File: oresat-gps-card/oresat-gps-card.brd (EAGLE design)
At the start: 99.8 x 94.6 mm, 373 parts, among them J1 ORESAT-DEBUG-CONNECTOR-CARD, J100 DM3BT-DSF-PEJS, J102 FTSH-105-XX-X-DV-K, J4 TFM-120-01-L-D-RA, Q1 MMBT2907, Q2 PMV45EN, Q3 DMP2240UDM, Q4 PMV45EN, Q5 MOSFET-PCH-SOT23-6, Q6 MOSFET-PCH-SOT23-6, U1 RCLAMP0504FB, U10 TLVH431, U11 TCAN330, U12 MIC842LYC5, U13 MIC842LYC5, U14 MAX4211FETE, U15 TPS62112, U16 MAX7310ATE, U17 25AAXX, U18 RCLAMP0504FB, U19 BP2G+, U2 TPS2051CDBVR, U20 MAX8510EXK29+T, U21 SF14-1575F5UUA1, U22 LT1719S6, U23 MAX2771ETI+, U24 VENUS838LPX-L, U3 THGBMJG7C2LBAU8, U4 SN74LVC1G07DCK, U5 SKY65723-81, U6 7Q-16.368MBG-T, U7 OSD3358-512M-BSM, U8 MAX8510EXK29+T, U9 MAX8510EXK29+T, Y1 24MHz, Y2 ABS07-32.768KHZ-T

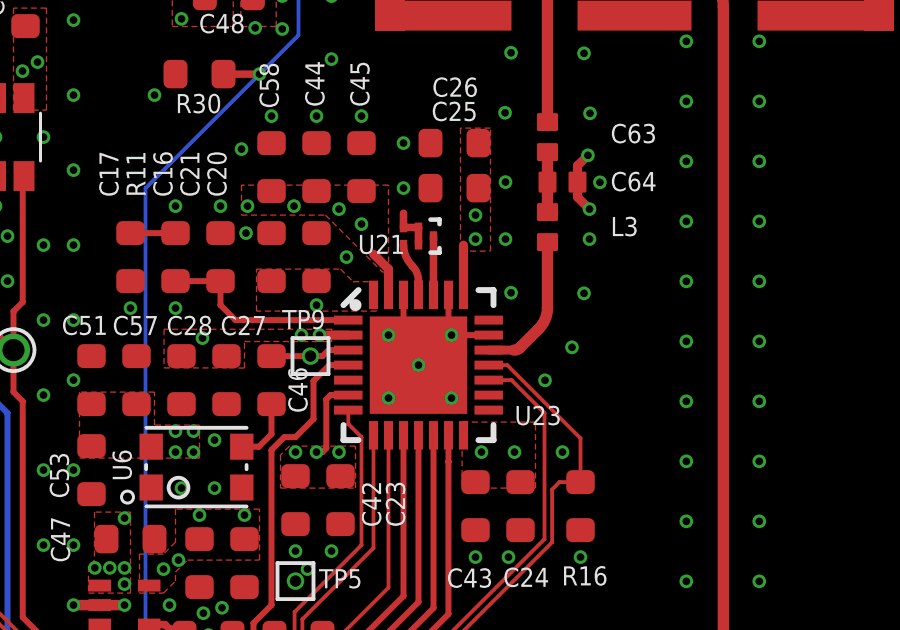
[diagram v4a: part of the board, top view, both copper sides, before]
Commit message: OK'd ERC errors.
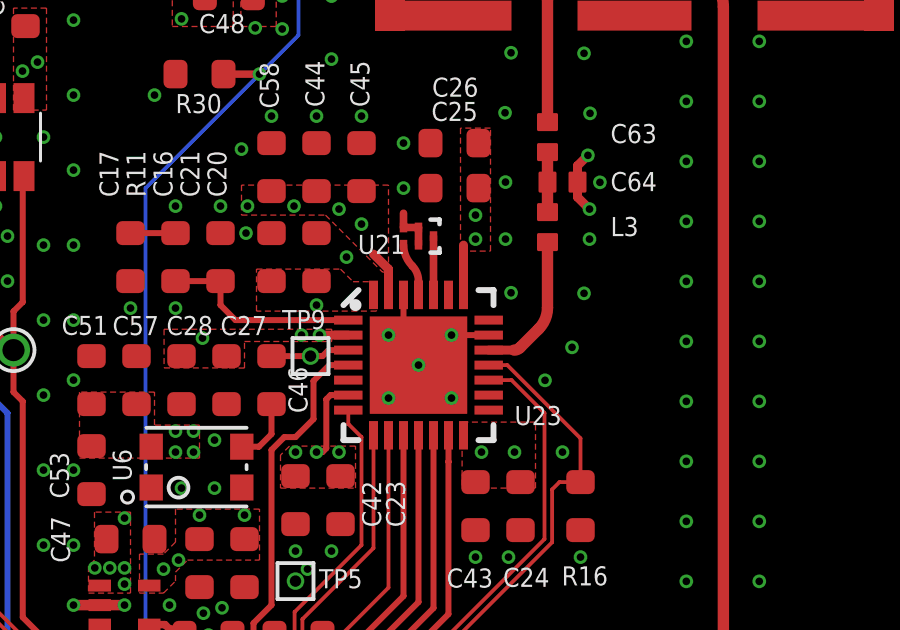
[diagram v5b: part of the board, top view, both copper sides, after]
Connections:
- net GND: no longer U23.23
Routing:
- net GND: track 43.6 -> 42.2 mm
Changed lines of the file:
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@@
 <?xml version="1.0" encoding="utf-8"?>
 <!DOCTYPE eagle SYSTEM "eagle.dtd">
-<eagle version="9.5.1">
+<eagle version="9.6.1">
 <drawing>
 <settings>
@@
 <attribute name="DPN" value="THGBMJG7C2LBAU8-ND" x="31.5" y="19.9" size="1.778" layer="27" display="off"/>
 <attribute name="MPN" value="THGBMJG7C2LBAU8" x="31.5" y="19.9" size="1.778" layer="27" display="off"/>
-<attribute name="NAME" x="35.925" y="27.0125" size="0.635" layer="25" font="vector" ratio="20"/>
 <attribute name="NAME" x="31.5" y="19.9" size="1.5" layer="33" ratio="15" align="center"/>
+<attribute name="NAME" x="35.925" y="27.0125" size="0.635" layer="25" font="vector" ratio="20"/>
 <attribute name="VALUE" x="25.9" y="12.3" size="0.8" layer="27" font="vector" ratio="15"/>
 </element>
@@
 <wire x1="64.475" y1="34.2" x2="65.3" y2="34.2" width="0.35" layer="1"/>
 <contactref element="U23" pad="20"/>
-<contactref element="U23" pad="23"/>
 <contactref element="U23" pad="26"/>
 <via x="67.2" y="38.1" extent="1-16" drill="0.254"/>
 <via x="68.3" y="38.1" extent="1-16" drill="0.254"/>
 <via x="72.7" y="45.8" extent="1-16" drill="0.254"/>
-<wire x1="76.1" y1="44.54" x2="76.1" y2="43.3" width="0.2" layer="1"/>
-<wire x1="76.1" y1="43.3" x2="76.2" y2="43.2" width="0.2" layer="1"/>
 <wire x1="74.6" y1="44.54" x2="74.6" y2="43.7" width="0.2" layer="1"/>
 <wire x1="74.6" y1="43.7" x2="74.1" y2="43.2" width="0.2" layer="1"/>
